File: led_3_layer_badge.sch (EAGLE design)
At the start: 42 parts, among them U1 ATMEGA168, U2 MCP73831, U3 AP34063, U4 PCA9952

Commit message: switched lipo charger to cheaper alt.
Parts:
- removed R2: 2k, rcl:R-US_R1206
- U2: value MCP73831 -> MCP73811
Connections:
- removed net N$2: C2.1, F1.2, LED1.A, U2.VIN
- net GND: no longer R2.2
- net N$6: now also C2.1, F1.2, LED1.A, U2.VIN; no longer R2.1
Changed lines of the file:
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@@
 <part name="GND2" library="sparkfun" deviceset="GND" device=""/>
 <part name="C1" library="adafruit" deviceset="C-US" device="C1206" value="100n"/>
-<part name="U2" library="sparkfun" deviceset="MCP73831" device=""/>
+<part name="U2" library="sparkfun" deviceset="MCP73831" device="" value="MCP73811"/>
 <part name="CN1" library="adafruit" deviceset="USB" device="MINIB"/>
 <part name="F1" library="sparkfun" deviceset="PTC" device="SMD"/>
 <part name="C2" library="adafruit" deviceset="C-US" device="C1206" value="4.7u"/>
 <part name="C3" library="adafruit" deviceset="C-US" device="C1206" value="4.7"/>
-<part name="R2" library="rcl" deviceset="R-US_" device="R1206" value="2k"/>
 <part name="R3" library="rcl" deviceset="R-US_" device="R1206" value="330"/>
 <part name="LED1" library="adafruit" deviceset="LED" device="SMT1206"/>
@@
 <part name="GND3" library="sparkfun" deviceset="GND" device=""/>
 <part name="GND4" library="sparkfun" deviceset="GND" device=""/>
-<part name="GND5" library="sparkfun" deviceset="GND" device=""/>
 <part name="GND6" library="sparkfun" deviceset="GND" device=""/>
 <part name="GND7" library="sparkfun" deviceset="GND" device=""/>
@@
 <instance part="C2" gate="G$1" x="43.18" y="73.66"/>
 <instance part="C3" gate="G$1" x="99.06" y="73.66"/>
-<instance part="R2" gate="G$1" x="93.98" y="73.66" rot="R270"/>
 <instance part="R3" gate="G$1" x="60.96" y="78.74"/>
 <instance part="LED1" gate="G$1" x="50.8" y="78.74" rot="R90"/>
@@
 <instance part="GND3" gate="1" x="43.18" y="63.5"/>
 <instance part="GND4" gate="1" x="88.9" y="63.5"/>
-<instance part="GND5" gate="1" x="93.98" y="63.5"/>
 <instance part="GND6" gate="1" x="99.06" y="63.5"/>
 <instance part="GND7" gate="1" x="104.14" y="63.5"/>
@@
 </segment>
 <segment>
-<pinref part="R2" gate="G$1" pin="2"/>
-<wire x1="93.98" y1="68.58" x2="93.98" y2="66.04" width="0.1524" layer="91"/>
-<pinref part="GND5" gate="1" pin="GND"/>
-</segment>
-<segment>
 <pinref part="C3" gate="G$1" pin="2"/>
 <wire x1="99.06" y1="68.58" x2="99.06" y2="66.04" width="0.1524" layer="91"/>
@@
 </segment>
 </net>
-<net name="N$2" class="0">
-<segment>
+<net name="N$4" class="0">
+<segment>
+<pinref part="R3" gate="G$1" pin="1"/>
+<pinref part="LED1" gate="G$1" pin="C"/>
+</segment>
+</net>
+<net name="N$5" class="0">
+<segment>
+<pinref part="R3" gate="G$1" pin="2"/>
+<pinref part="U2" gate="G$1" pin="STAT"/>
+</segment>
+</net>
+<net name="N$6" class="0">
+<segment>
+<pinref part="U2" gate="G$1" pin="PROG"/>
+<wire x1="86.36" y1="81.28" x2="88.9" y2="81.28" width="0.1524" layer="91"/>
+<wire x1="88.9" y1="81.28" x2="88.9" y2="91.44" width="0.1524" layer="91"/>
 <pinref part="F1" gate="G$1" pin="2"/>
 <pinref part="C2" gate="G$1" pin="1"/>
@@
 <wire x1="45.72" y1="78.74" x2="48.26" y2="78.74" width="0.1524" layer="91"/>
 <pinref part="U2" gate="G$1" pin="VIN"/>
-<wire x1="45.72" y1="83.82" x2="66.04" y2="83.82" width="0.1524" layer="91"/>
+<wire x1="45.72" y1="83.82" x2="63.5" y2="83.82" width="0.1524" layer="91"/>
 <junction x="45.72" y="83.82"/>
 <junction x="43.18" y="83.82"/>
-</segment>
-</net>
-<net name="N$4" class="0">
-<segment>
-<pinref part="R3" gate="G$1" pin="1"/>
-<pinref part="LED1" gate="G$1" pin="C"/>
-</segment>
-</net>
-<net name="N$5" class="0">
-<segment>
-<pinref part="R3" gate="G$1" pin="2"/>
-<pinref part="U2" gate="G$1" pin="STAT"/>
-</segment>
-</net>
-<net name="N$6" class="0">
-<segment>
-<pinref part="U2" gate="G$1" pin="PROG"/>
-<pinref part="R2" gate="G$1" pin="1"/>
-<wire x1="86.36" y1="81.28" x2="93.98" y2="81.28" width="0.1524" layer="91"/>
-<wire x1="93.98" y1="81.28" x2="93.98" y2="78.74" width="0.1524" layer="91"/>
-</segment>
-</net>
+<wire x1="63.5" y1="83.82" x2="66.04" y2="83.82" width="0.1524" layer="91"/>
+<wire x1="88.9" y1="91.44" x2="63.5" y2="91.44" width="0.1524" layer="91"/>
+<wire x1="63.5" y1="91.44" x2="63.5" y2="83.82" width="0.1524" layer="91"/>
+<junction x="63.5" y="83.82"/>
+</segment>
+</net>

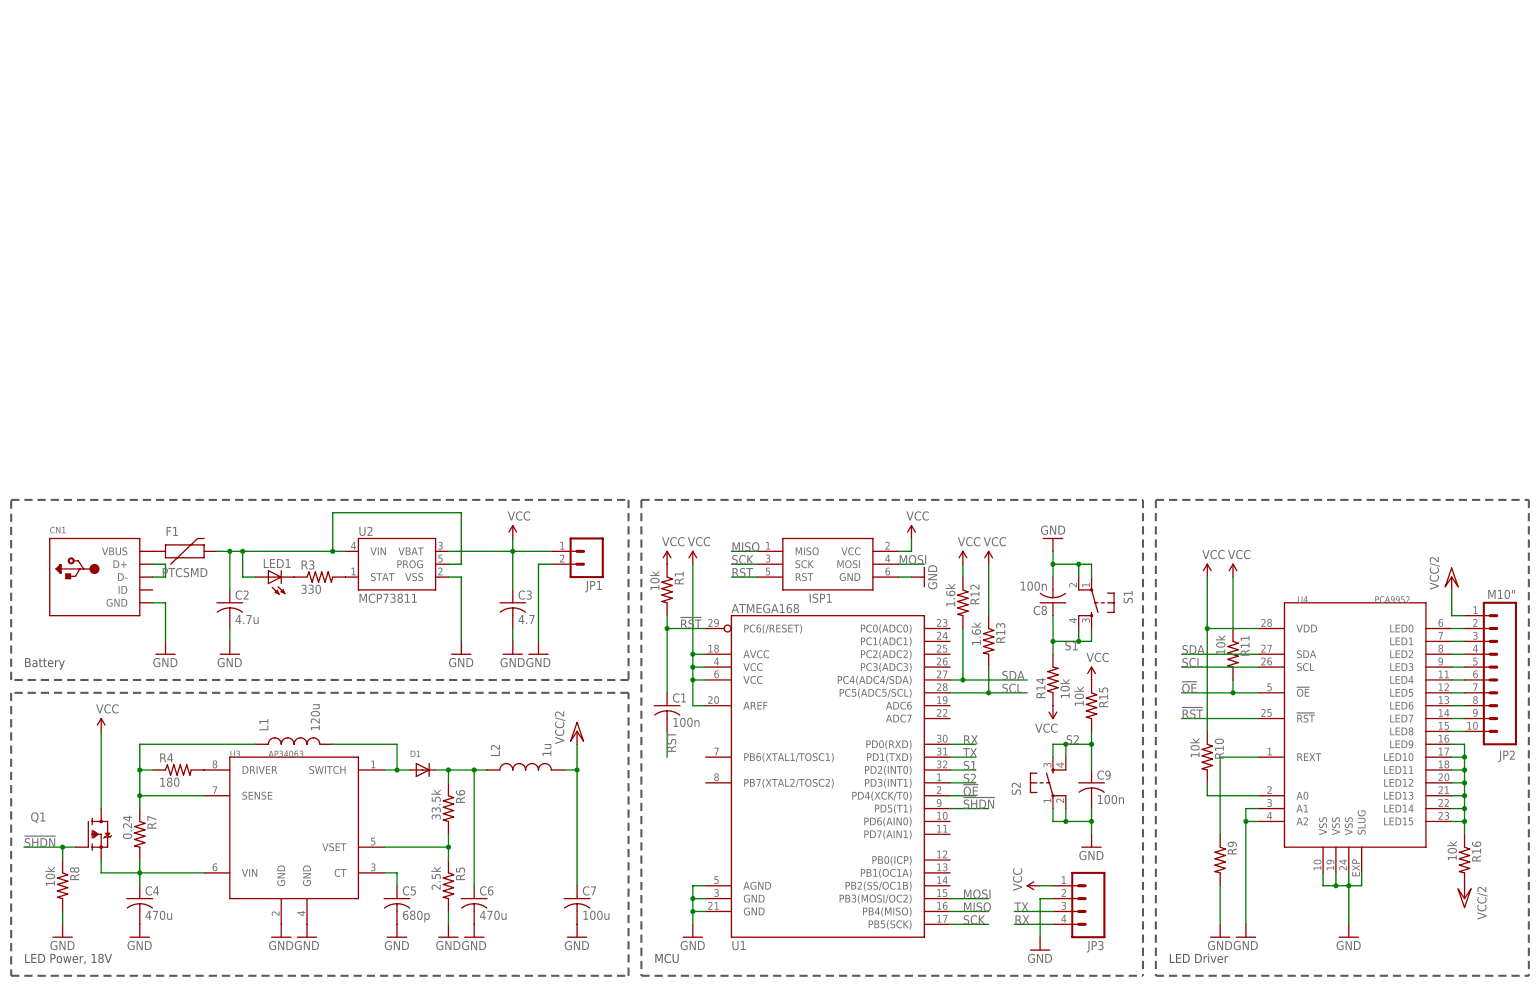
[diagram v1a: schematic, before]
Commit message: Updated board for 4-string design, single double sided board.
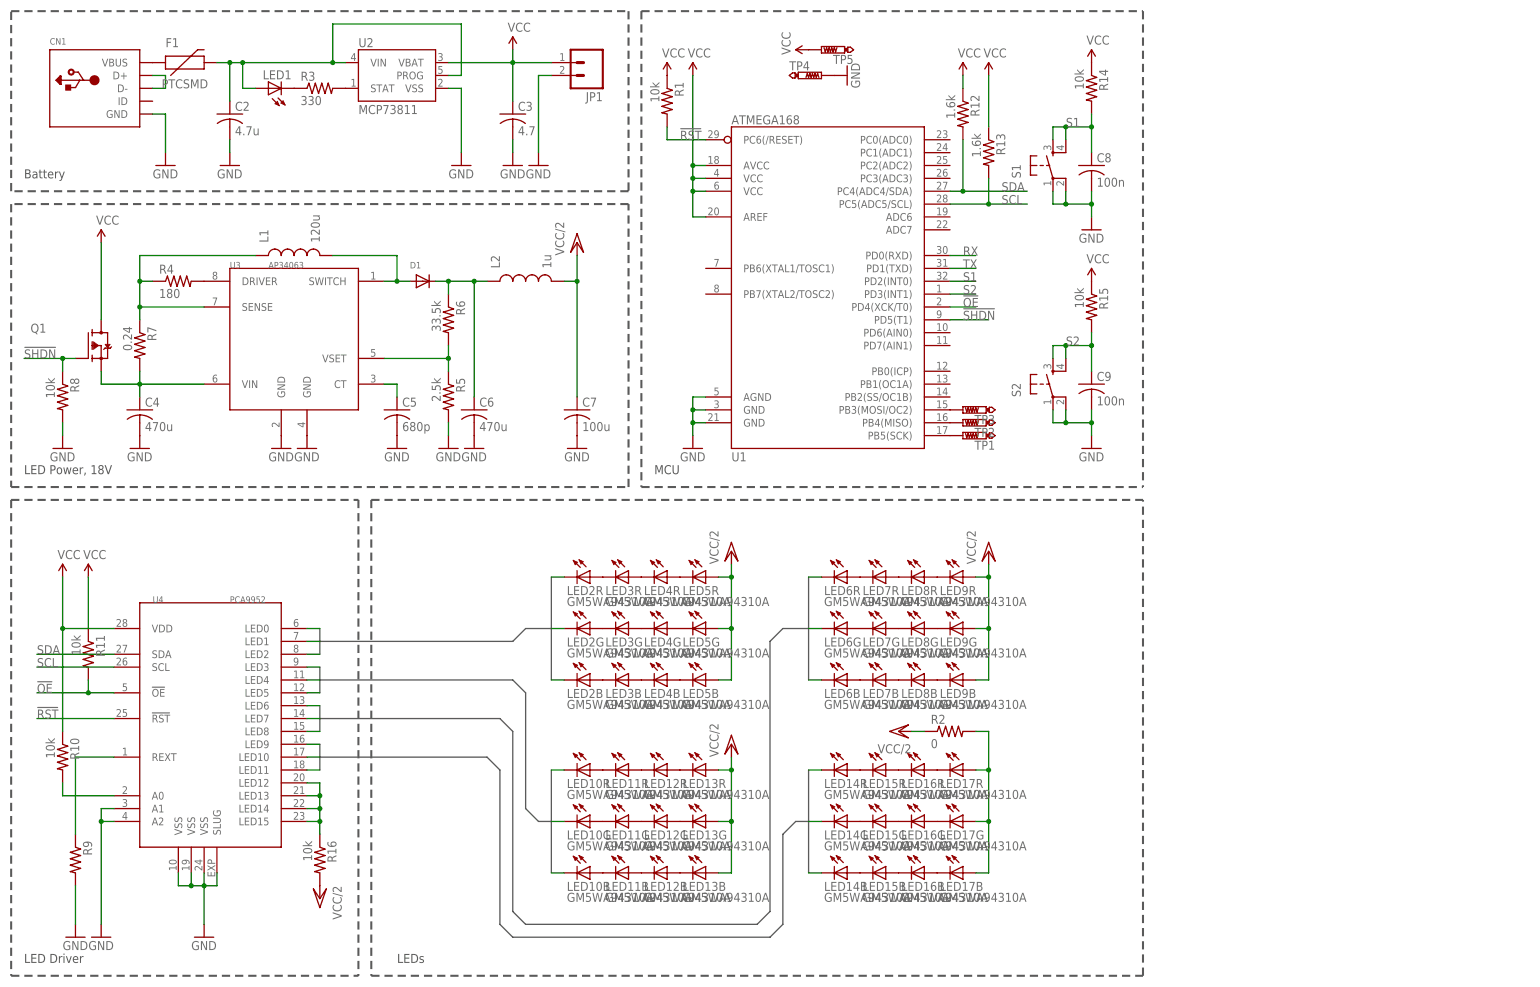
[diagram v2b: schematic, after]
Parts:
- removed C1: 100n, adafruit:C-USC1206
- removed ISP1: AVRISP-6, adafruit:AVRISP-6
- removed JP2: M10", sparkfun:M10"
- removed JP3: (no value), sparkfun:M04PTH
- added LED10, LED11, LED12, LED13, LED14, LED15, LED16, LED17, LED2, LED3, LED4, LED5, LED6, LED7, LED8, LED9: GM5WA94310A, led:GM5WA94310A
- added R2: 0, rcl:R-US_R1206
- added TP1, TP2, TP3, TP4, TP5: PTR1TP13R, testpad:PTR1TP13R
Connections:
- removed net MISO: ISP1.MISO, U1.PB4(MISO)
- removed net MOSI: ISP1.MOSI, U1.PB3(MOSI/OC2)
- removed net RST: C1.2, ISP1.RST
- removed net SCK: ISP1.SCK, U1.PB5(SCK)
- new net A0: LED2R.C, U4.LED0
- new net A1: LED2G.C, U4.LED1
- new net A2: LED2B.C, U4.LED2
- new net B0: LED10R.C, U4.LED3
- new net B1: LED10G.C, U4.LED4
- new net B2: LED10B.C, U4.LED5
- new net C0: LED6R.C, U4.LED6
- new net C1: LED6G.C, U4.LED7
- new net C2: LED6B.C, U4.LED8
- new net D0: LED14R.C, U4.LED9
- new net D1: LED14G.C, U4.LED10
- new net D2: LED14B.C, U4.LED11
- new net N$2: LED2R.A, LED3R.C
- new net N$24: LED2G.A, LED3G.C
- new net N$25: LED2B.A, LED3B.C
- new net N$28: LED4R.A, LED5R.C
- new net N$29: LED4G.A, LED5G.C
- new net N$30: LED4B.A, LED5B.C
- new net N$31: LED3R.A, LED4R.C
- new net N$32: LED3G.A, LED4G.C
- new net N$33: LED3B.A, LED4B.C
- new net N$34: LED7B.A, LED8B.C
- new net N$35: LED10R.A, LED11R.C
- new net N$36: LED10G.A, LED11G.C
- new net N$37: LED10B.A, LED11B.C
- new net N$38: LED12R.A, LED13R.C
- new net N$39: LED12G.A, LED13G.C
- new net N$40: LED12B.A, LED13B.C
- new net N$41: LED11R.A, LED12R.C
- new net N$42: LED11G.A, LED12G.C
- new net N$43: LED11B.A, LED12B.C
- new net N$44: LED14R.A, LED15R.C
- new net N$45: LED14G.A, LED15G.C
- new net N$46: LED14B.A, LED15B.C
- new net N$47: LED16R.A, LED17R.C
- new net N$48: LED16G.A, LED17G.C
- new net N$49: LED16B.A, LED17B.C
- new net N$50: LED15R.A, LED16R.C
- new net N$51: LED15G.A, LED16G.C
- new net N$52: LED15B.A, LED16B.C
- new net N$53: TP1.TP, U1.PB5(SCK)
- new net N$54: TP2.TP, U1.PB4(MISO)
- new net N$55: TP3.TP, U1.PB3(MOSI/OC2)
- net !RST: no longer C1.1
- net GND: now also TP4.TP; no longer ISP1.GND, JP3.2
- net N$10: now also LED17B.A, LED17G.A, LED17R.A, R2.2; no longer JP2.2, U4.LED0
- net N$12: now also LED6R.A, LED7R.C; no longer JP2.3, U4.LED1
- net N$16: now also LED6G.A, LED7G.C; no longer JP2.4, U4.LED2
- net N$17: now also LED6B.A, LED7B.C; no longer JP2.5, U4.LED3
- net N$18: now also LED8R.A, LED9R.C; no longer JP2.6, U4.LED4
- net N$19: now also LED8G.A, LED9G.C; no longer JP2.7, U4.LED5
- net N$20: now also LED8B.A, LED9B.C; no longer JP2.8, U4.LED6
- net N$21: now also LED7R.A, LED8R.C; no longer JP2.9, U4.LED7
- net N$22: now also LED7G.A, LED8G.C; no longer JP2.10, U4.LED8
- net N$23: no longer U4.LED10, U4.LED11, U4.LED9
- net RX: no longer JP3.4
- net TX: no longer JP3.3
- net VCC: now also TP5.TP; no longer ISP1.VCC, JP3.1
- net VCC/2: now also LED13B.A, LED13G.A, LED13R.A, LED5B.A, LED5G.A, LED5R.A, LED9B.A, LED9G.A, LED9R.A, R2.1; no longer JP2.1
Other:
- note added: "LEDs"
- moved on the sheet: C2, C3, C4, C5, C6, C7, C8, C9, CN1, D1, F1, JP1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
